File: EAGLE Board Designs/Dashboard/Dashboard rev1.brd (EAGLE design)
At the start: 67.9 x 27.6 mm, 47 parts, among them IC1 LM340S, J1 AVR-ISP-HEADER, U1 ATMEGA328P-AU, X1 CONNECTOR-6NANO-FIT_VERTICAL-6

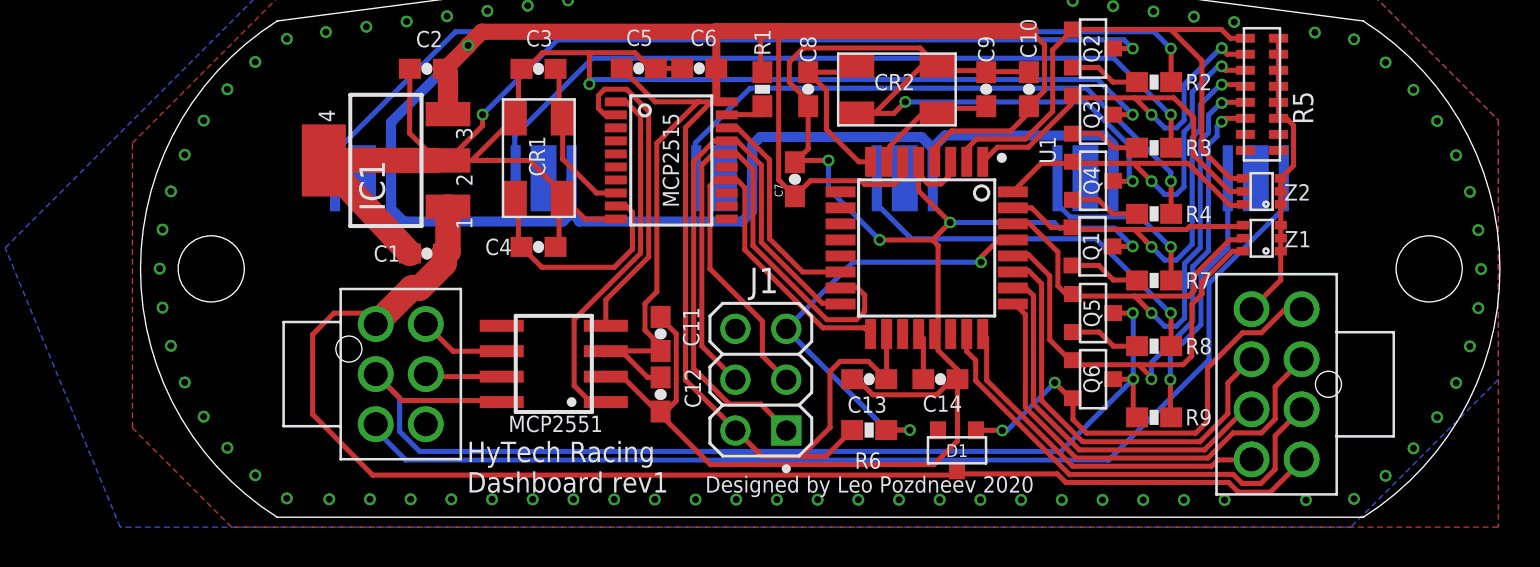
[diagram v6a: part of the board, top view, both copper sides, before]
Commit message: made changes for osh park
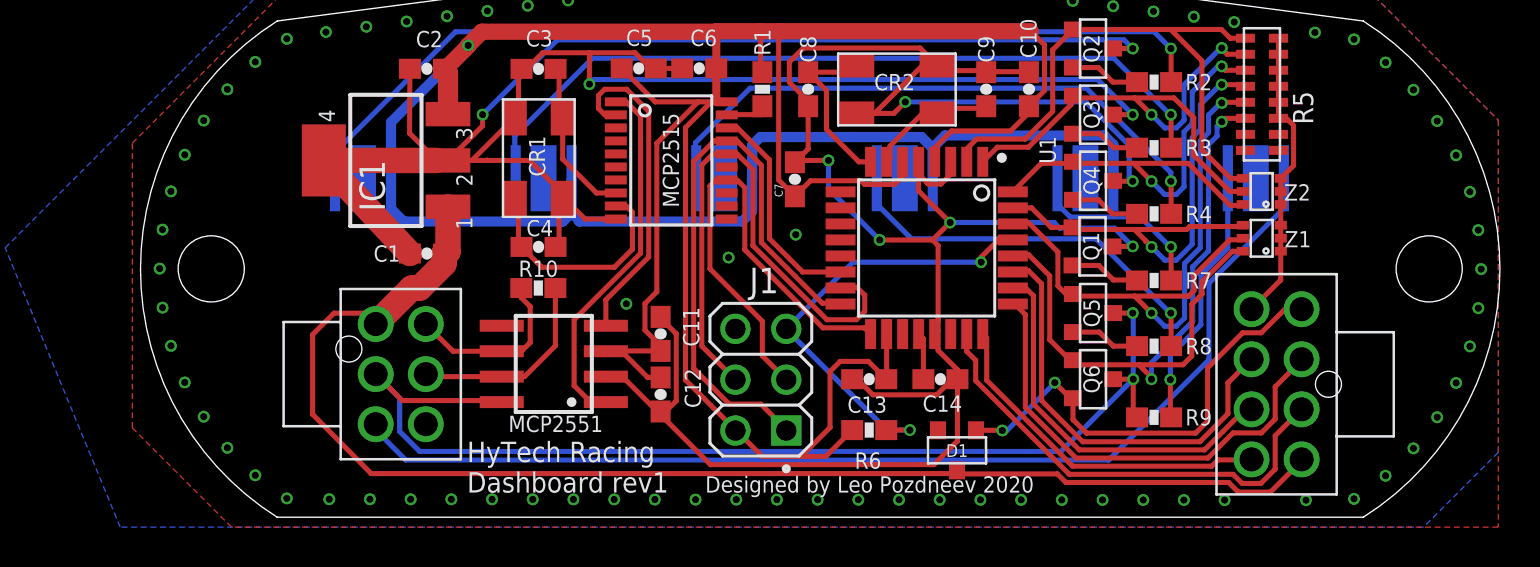
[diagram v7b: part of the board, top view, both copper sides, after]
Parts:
- added R10: 120, HyTechDevices:0603-RES
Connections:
- net CANH: now also R10.1
- net CANL: now also R10.2
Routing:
- net CANH: track 3.84 -> 10.0 mm
- net CANL: track 4.35 -> 8.86 mm
- net GND: vias 79 -> 93
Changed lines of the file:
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@@
 </element>
 <element name="C4" library="HyTechDevices" package="0603-CAP" value="14pF" x="13.0396" y="13.4833" smashed="yes">
-<attribute name="NAME" x="10.3726" y="13.0769" size="0.8128" layer="25" font="vector"/>
+<attribute name="NAME" x="12.43" y="14.0167" size="0.8128" layer="25" font="vector"/>
 </element>
 <element name="C3" library="HyTechDevices" package="0603-CAP" value="14pF" x="13.0396" y="22.3733" smashed="yes">
@@
 <attribute name="NAME" x="33.9344" y="2.9972" size="0.635" layer="25" rot="R180" align="top-center"/>
 <attribute name="VALUE" x="32.5374" y="2.4384" size="0.3048" layer="27" rot="R180" align="bottom-center"/>
+</element>
+<element name="R10" library="HyTechDevices" package="0603-RES" value="120" x="13.0302" y="11.43" smashed="yes" rot="R180">
+<attribute name="NAME" x="14.0208" y="12.8016" size="0.8128" layer="25" font="vector" rot="R180"/>
+<attribute name="VALUE" x="13.8938" y="12.446" size="0.4064" layer="27" font="vector" rot="R180"/>
 </element>
 </elements>
@@
 <vertex x="53.086" y="27.686"/>
 <vertex x="60.96" y="19.812"/>
-<vertex x="60.96" y="6.858"/>
-<vertex x="53.594" y="-0.508"/>
+<vertex x="60.96" y="3.2258"/>
+<vertex x="57.2262" y="-0.508"/>
 <vertex x="-7.8486" y="-0.508"/>
 </polygon>
@@
 <via x="47.294778125" y="0.844403125" extent="1-16" drill="0.35"/>
 <via x="51.358778125" y="0.840528125" extent="1-16" drill="0.35"/>
+<via x="16.790703125" y="26.125225" extent="1-16" drill="0.35"/>
+<via x="18.884815625" y="26.338234375" extent="1-16" drill="0.35"/>
+<via x="20.9079875" y="26.55230625" extent="1-16" drill="0.35"/>
+<via x="23.0621875" y="26.691125" extent="1-16" drill="0.35"/>
+<via x="25.11759375" y="26.78000625" extent="1-16" drill="0.35"/>
+<via x="27.17456875" y="26.81889375" extent="1-16" drill="0.35"/>
+<via x="29.1810875" y="26.78236875" extent="1-16" drill="0.35"/>
+<via x="31.212115625" y="26.7212375" extent="1-16" drill="0.35"/>
+<via x="33.241025" y="26.584734375" extent="1-16" drill="0.35"/>
+<via x="35.241184375" y="26.398325" extent="1-16" drill="0.35"/>
+<via x="37.36376875" y="26.1367125" extent="1-16" drill="0.35"/>
+<via x="22.5298" y="12.954" extent="1-16" drill="0.35"/>
+<via x="25.8826" y="14.097" extent="1-16" drill="0.35"/>
+<via x="17.4244" y="10.6426" extent="1-16" drill="0.35"/>
 </signal>
 <signal name="+5V">
@@
 <wire x1="11.2016" y1="8.2763" x2="8.7686" y2="8.2763" width="0.254" layer="1"/>
 <wire x1="8.7686" y1="8.2763" x2="7.4116" y2="9.6333" width="0.254" layer="1"/>
+<contactref element="R10" pad="2"/>
+<wire x1="11.2016" y1="8.2763" x2="11.2565" y2="8.3312" width="0.254" layer="1"/>
+<wire x1="12.6238" y1="10.5038" x2="12.1802" y2="10.9474" width="0.254" layer="1"/>
+<wire x1="12.1802" y1="10.9474" x2="12.1802" y2="11.43" width="0.254" layer="1"/>
+<wire x1="11.2565" y1="8.3312" x2="12.2428" y2="8.3312" width="0.254" layer="1"/>
+<wire x1="12.2428" y1="8.3312" x2="12.6238" y2="8.7122" width="0.254" layer="1"/>
+<wire x1="12.6238" y1="8.7122" x2="12.6238" y2="10.5038" width="0.254" layer="1"/>
 </signal>
 <signal name="CANH">
@@
 <wire x1="11.2016" y1="7.0063" x2="7.5386" y2="7.0063" width="0.254" layer="1"/>
 <wire x1="7.5386" y1="7.0063" x2="7.4116" y2="7.1333" width="0.254" layer="1"/>
+<contactref element="R10" pad="1"/>
+<wire x1="11.2016" y1="7.0063" x2="11.2057" y2="7.0104" width="0.254" layer="1"/>
+<wire x1="11.2057" y1="7.0104" x2="12.3444" y2="7.0104" width="0.254" layer="1"/>
+<wire x1="12.3444" y1="7.0104" x2="13.8802" y2="8.5462" width="0.254" layer="1"/>
+<wire x1="13.8802" y1="8.5462" x2="13.8802" y2="11.43" width="0.254" layer="1"/>
 </signal>
 <signal name="N$5">
@@
 <wire x1="7.112" y1="11.43" x2="8.3176" y2="12.6356" width="1.27" layer="1"/>
 <wire x1="8.3176" y1="12.6356" x2="8.3176" y2="13.1531" width="1.27" layer="1"/>
-<wire x1="1.762" y1="5.124375" x2="4.758734375" y2="2.0907" width="0.254" layer="1"/>
+<wire x1="1.762" y1="5.124375" x2="4.6834625" y2="2.1669" width="0.254" layer="1"/>
 <contactref element="D1" pad="3"/>
 <wire x1="38.94521875" y1="2.1496" x2="34.1122" y2="2.1496" width="0.254" layer="1"/>
 <wire x1="34.1122" y1="2.1496" x2="33.9344" y2="2.3274" width="0.254" layer="1"/>
 <wire x1="39.37171875" y1="1.7231" x2="38.94521875" y2="2.1496" width="0.254" layer="1"/>
-<wire x1="33.9344" y1="2.3274" x2="33.6977" y2="2.0907" width="0.254" layer="1"/>
-<wire x1="33.6977" y1="2.0907" x2="4.758734375" y2="2.0907" width="0.254" layer="1"/>
+<wire x1="33.9344" y1="2.3274" x2="33.7739" y2="2.1669" width="0.254" layer="1"/>
+<wire x1="33.7739" y1="2.1669" x2="4.6834625" y2="2.1669" width="0.254" layer="1"/>
 <wire x1="47.9809375" y1="1.2405" x2="47.4983375" y2="1.7231" width="0.254" layer="1"/>
 <wire x1="51.1396" y1="2.8753" x2="51.0126" y2="2.7483" width="0.254" layer="1"/>
@@
 <wire x1="40.21340625" y1="3.7551" x2="38.158" y2="5.81050625" width="0.254" layer="1"/>
 </signal>
-<signal name="N$14">
-<via x="37.36376875" y="26.1367125" extent="1-16" drill="0.35"/>
-</signal>
-<signal name="N$20">
-<via x="35.241184375" y="26.398325" extent="1-16" drill="0.35"/>
-</signal>
-<signal name="N$21">
-<via x="33.241025" y="26.584734375" extent="1-16" drill="0.35"/>
-</signal>
-<signal name="N$22">
-<via x="31.212115625" y="26.7212375" extent="1-16" drill="0.35"/>
-</signal>
-<signal name="N$23">
-<via x="29.1810875" y="26.78236875" extent="1-16" drill="0.35"/>
-</signal>
-<signal name="N$24">
-<via x="27.17456875" y="26.81889375" extent="1-16" drill="0.35"/>
-</signal>
-<signal name="N$25">
-<via x="25.11759375" y="26.78000625" extent="1-16" drill="0.35"/>
-</signal>
-<signal name="N$26">
-<via x="23.0621875" y="26.691125" extent="1-16" drill="0.35"/>
-</signal>
-<signal name="N$27">
-<via x="20.9079875" y="26.55230625" extent="1-16" drill="0.35"/>
-</signal>
-<signal name="N$28">
-<via x="18.884815625" y="26.338234375" extent="1-16" drill="0.35"/>
-</signal>
-<signal name="N$29">
-<via x="16.790703125" y="26.125225" extent="1-16" drill="0.35"/>
-</signal>
 </signals>

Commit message: added values to LED resistors
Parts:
- C3, C4, C8, C9: value 14pF -> 15pF
- R2, R4: value (none) -> 10
- R3, R7, R8, R9: value (none) -> 14.7
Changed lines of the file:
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@@
 <drawing>
 <settings>
-<setting alwaysvectorfont="yes"/>
+<setting alwaysvectorfont="no"/>
 <setting verticaltext="up"/>
 </settings>
@@
 <attribute name="VALUE" x="23.9616" y="13.9913" size="0.8128" layer="22" rot="MR0"/>
 </element>
-<element name="C4" library="HyTechDevices" package="0603-CAP" value="14pF" x="13.0396" y="13.4833" smashed="yes">
+<element name="C4" library="HyTechDevices" package="0603-CAP" value="15pF" x="13.0396" y="13.4833" smashed="yes">
 <attribute name="NAME" x="12.43" y="14.0167" size="0.8128" layer="25" font="vector"/>
 </element>
-<element name="C3" library="HyTechDevices" package="0603-CAP" value="14pF" x="13.0396" y="22.3733" smashed="yes">
+<element name="C3" library="HyTechDevices" package="0603-CAP" value="15pF" x="13.0396" y="22.3733" smashed="yes">
 <attribute name="NAME" x="12.4046" y="23.4909" size="0.8128" layer="25" font="vector"/>
 </element>
-<element name="C9" library="HyTechDevices" package="0603-CAP" value="14pF" x="35.3916" y="21.3573" smashed="yes" rot="R270">
+<element name="C9" library="HyTechDevices" package="0603-CAP" value="15pF" x="35.3916" y="21.3573" smashed="yes" rot="R270">
 <attribute name="NAME" x="34.9852" y="24.0243" size="0.8128" layer="25" font="vector" rot="R270"/>
 </element>
-<element name="C8" library="HyTechDevices" package="0603-CAP" value="14pF" x="26.5016" y="21.3573" smashed="yes" rot="R270">
+<element name="C8" library="HyTechDevices" package="0603-CAP" value="15pF" x="26.5016" y="21.3573" smashed="yes" rot="R270">
 <attribute name="NAME" x="26.0952" y="24.0243" size="0.8128" layer="25" font="vector" rot="R270"/>
 </element>
@@
 <attribute name="NAME" x="24.622" y="23.0337" size="0.8128" layer="25" font="vector" rot="R90"/>
 </element>
-<element name="R2" library="HyTechDevices" package="0603-RES" value="" x="43.7736" y="21.7129" smashed="yes" rot="R180">
+<element name="R2" library="HyTechDevices" package="0603-RES" value="10" x="43.7736" y="21.7129" smashed="yes" rot="R180">
 <attribute name="NAME" x="46.6692" y="22.1193" size="0.8128" layer="25" font="vector" rot="R180"/>
 <attribute name="VALUE" x="44.6372" y="22.7289" size="0.4064" layer="27" font="vector" rot="R180"/>
@@
 <attribute name="NAME" x="50.7044" y="21.2633" size="1.016" layer="25" font="vector" rot="R270"/>
 </element>
-<element name="R4" library="HyTechDevices" package="0603-RES" value="" x="43.7736" y="15.1343" smashed="yes" rot="R180">
+<element name="R4" library="HyTechDevices" package="0603-RES" value="10" x="43.7736" y="15.1343" smashed="yes" rot="R180">
 <attribute name="NAME" x="46.6692" y="15.5407" size="0.8128" layer="25" font="vector" rot="R180"/>
 <attribute name="VALUE" x="44.6372" y="16.1503" size="0.4064" layer="27" font="vector" rot="R180"/>
 </element>
-<element name="R3" library="HyTechDevices" package="0603-RES" value="" x="43.7736" y="18.4363" smashed="yes" rot="R180">
+<element name="R3" library="HyTechDevices" package="0603-RES" value="14.7" x="43.7736" y="18.4363" smashed="yes" rot="R180">
 <attribute name="NAME" x="46.6692" y="18.8427" size="0.8128" layer="25" font="vector" rot="R180"/>
 <attribute name="VALUE" x="44.6372" y="19.4523" size="0.4064" layer="27" font="vector" rot="R180"/>
 </element>
-<element name="R8" library="HyTechDevices" package="0603-RES" value="" x="43.7736" y="8.5303" smashed="yes" rot="R180">
+<element name="R8" library="HyTechDevices" package="0603-RES" value="14.7" x="43.7736" y="8.5303" smashed="yes" rot="R180">
 <attribute name="NAME" x="46.6692" y="8.9367" size="0.8128" layer="25" font="vector" rot="R180"/>
 <attribute name="VALUE" x="44.6372" y="9.5463" size="0.4064" layer="27" font="vector" rot="R180"/>
 </element>
-<element name="R9" library="HyTechDevices" package="0603-RES" value="" x="43.7736" y="4.9743" smashed="yes" rot="R180">
+<element name="R9" library="HyTechDevices" package="0603-RES" value="14.7" x="43.7736" y="4.9743" smashed="yes" rot="R180">
 <attribute name="NAME" x="46.6692" y="5.3807" size="0.8128" layer="25" font="vector" rot="R180"/>
 <attribute name="VALUE" x="44.6372" y="5.9903" size="0.4064" layer="27" font="vector" rot="R180"/>
 </element>
-<element name="R7" library="HyTechDevices" package="0603-RES" value="" x="43.7736" y="11.8069" smashed="yes" rot="R180">
+<element name="R7" library="HyTechDevices" package="0603-RES" value="14.7" x="43.7736" y="11.8069" smashed="yes" rot="R180">
 <attribute name="NAME" x="46.6692" y="12.2133" size="0.8128" layer="25" font="vector" rot="R180"/>
 <attribute name="VALUE" x="44.6372" y="12.8229" size="0.4064" layer="27" font="vector" rot="R180"/>
